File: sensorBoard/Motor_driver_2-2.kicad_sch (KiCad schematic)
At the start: 13 parts, among them Q17 BSC440N10NS3G, Q5 BSC440N10NS3G, Q6 BSC440N10NS3G, Q7 BSC440N10NS3G, U11 4N25, U29 4N25, U6 4011, U8 4011

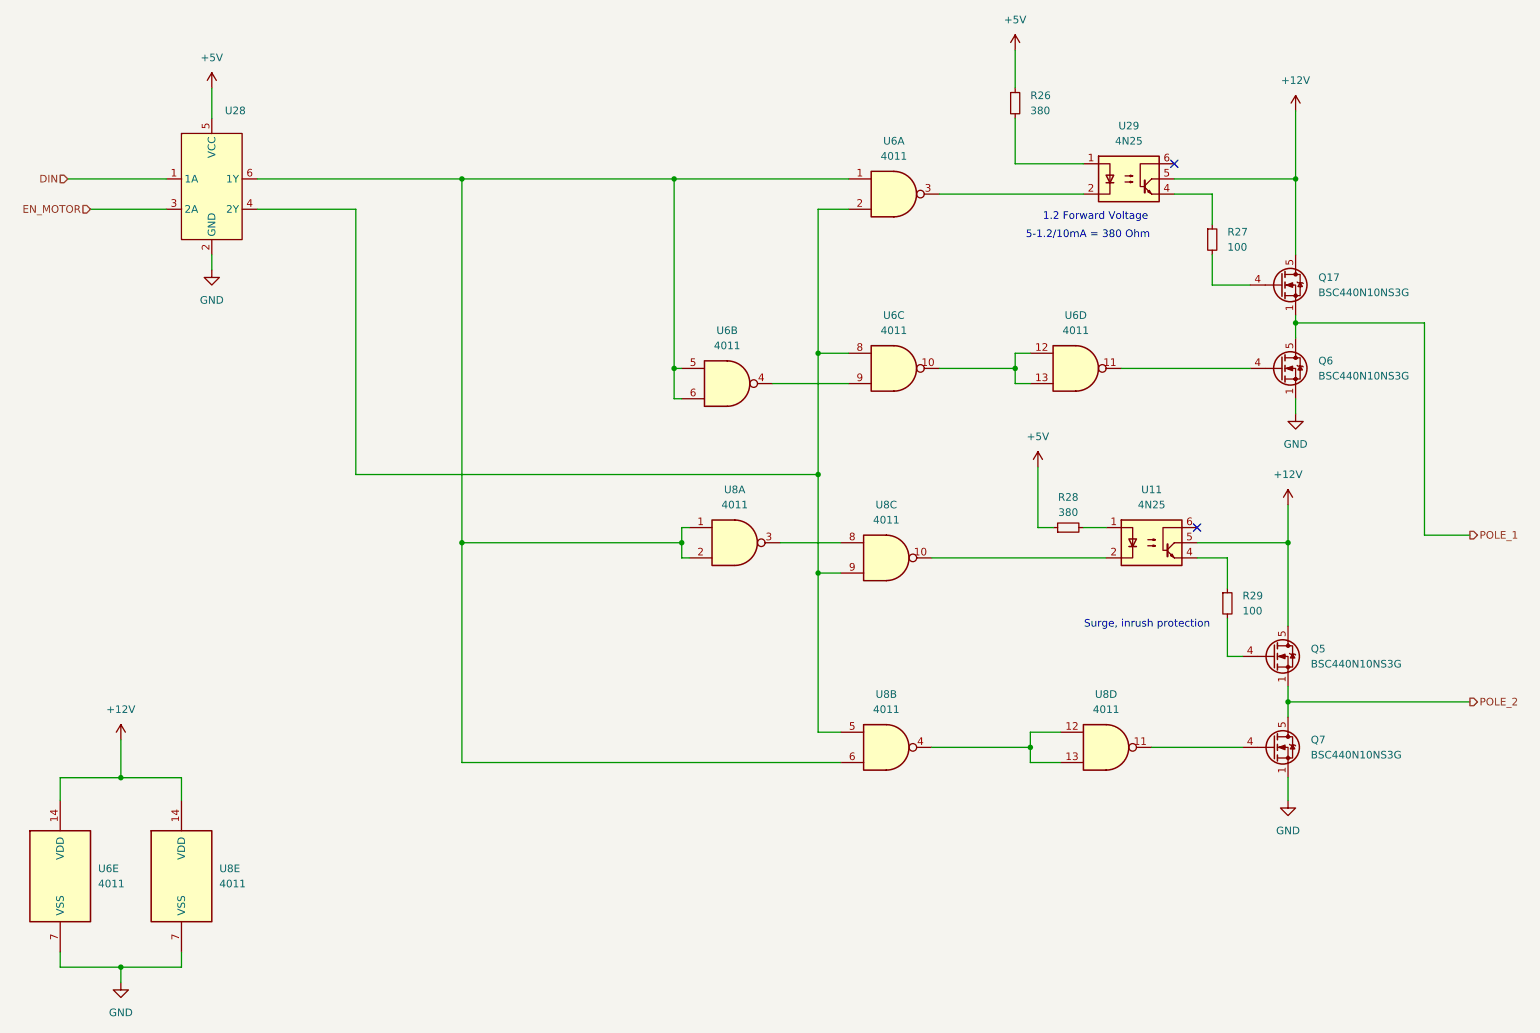
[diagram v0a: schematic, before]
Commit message: new two separate pcbs
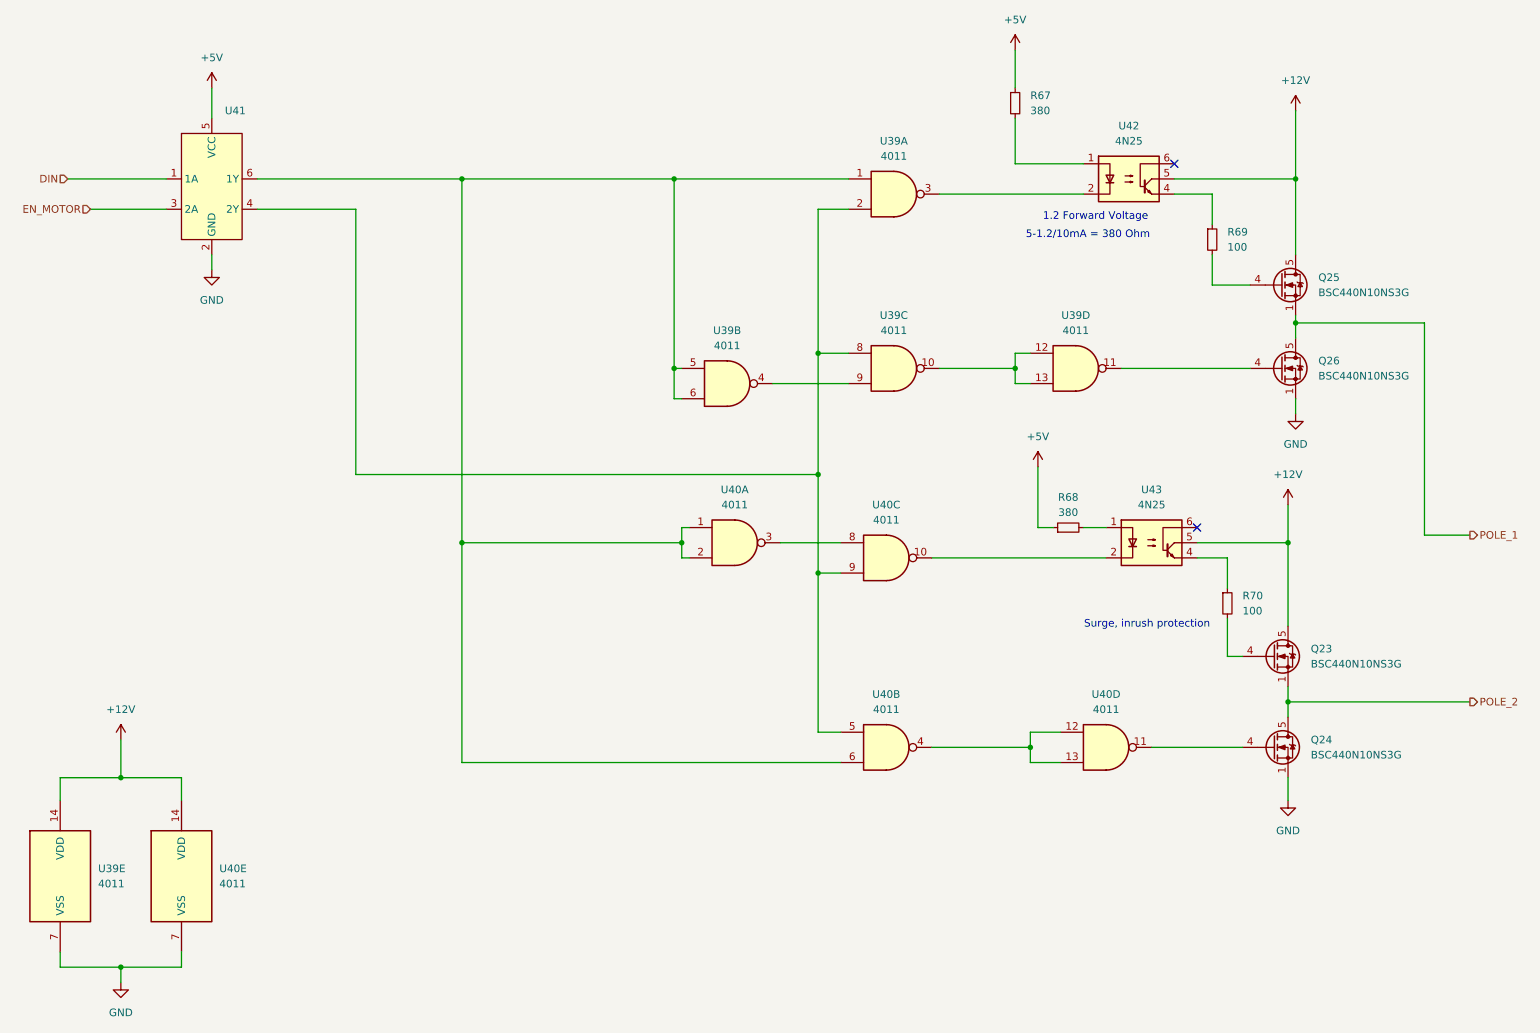
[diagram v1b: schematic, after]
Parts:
- renumbered Q5 to Q23, Q7 to Q24, Q17 to Q25, Q6 to Q26, R26 to R67, R28 to R68, R27 to R69, R29 to R70, U6 to U39, U8 to U40, U28 to U41, U29 to U42, U11 to U43
